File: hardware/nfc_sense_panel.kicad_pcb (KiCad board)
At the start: 4 copper layers, 105 x 103.3 mm, 538 parts, among them U1 TMP117AIDRVR, U2 RF430CL330HIRGTR‎, U3 ATtiny1626-MFR

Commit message: penel mousebite spacing
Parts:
- added KiKit_MB_10_9: NPTH, NPTH, F.Cu at (150.0, 27.0)
- added KiKit_MB_11_9: NPTH, NPTH, F.Cu at (147.0, 69.8)
- added KiKit_MB_12_9: NPTH, NPTH, F.Cu at (160.8, 47.1)
- added KiKit_MB_13_9: NPTH, NPTH, F.Cu at (179.4, 50.1)
- added KiKit_MB_14_9: NPTH, NPTH, F.Cu at (171.6, 27.0)
- added KiKit_MB_15_9: NPTH, NPTH, F.Cu at (168.6, 69.8)
- added KiKit_MB_16_9: NPTH, NPTH, F.Cu at (182.4, 47.1)
- added KiKit_MB_17_9: NPTH, NPTH, F.Cu at (193.2, 27.0)
- added KiKit_MB_18_9: NPTH, NPTH, F.Cu at (190.2, 69.8)
- added KiKit_MB_19_9: NPTH, NPTH, F.Cu at (114.6, 96.2)
- added KiKit_MB_1_9: NPTH, NPTH, F.Cu at (114.6, 50.1)
- added KiKit_MB_20_9: NPTH, NPTH, F.Cu at (106.8, 73.1)
- added KiKit_MB_21_9: NPTH, NPTH, F.Cu at (103.8, 116.0)
- added KiKit_MB_22_9: NPTH, NPTH, F.Cu at (117.6, 93.2)
- added KiKit_MB_23_9: NPTH, NPTH, F.Cu at (136.2, 96.2)
- added KiKit_MB_24_9: NPTH, NPTH, F.Cu at (128.4, 73.1)
- added KiKit_MB_25_9: NPTH, NPTH, F.Cu at (125.4, 116.0)
- added KiKit_MB_26_9: NPTH, NPTH, F.Cu at (139.2, 93.2)
- added KiKit_MB_27_9: NPTH, NPTH, F.Cu at (157.8, 96.2)
- added KiKit_MB_28_9: NPTH, NPTH, F.Cu at (150.0, 73.1)
- added KiKit_MB_29_9: NPTH, NPTH, F.Cu at (147.0, 116.0)
- added KiKit_MB_2_9: NPTH, NPTH, F.Cu at (106.8, 27.0)
- added KiKit_MB_30_9: NPTH, NPTH, F.Cu at (160.8, 93.2)
- added KiKit_MB_31_9: NPTH, NPTH, F.Cu at (179.4, 96.2)
- added KiKit_MB_32_9: NPTH, NPTH, F.Cu at (171.6, 73.1)
- added KiKit_MB_33_9: NPTH, NPTH, F.Cu at (168.6, 116.0)
- added KiKit_MB_34_9: NPTH, NPTH, F.Cu at (182.4, 93.2)
- added KiKit_MB_35_9: NPTH, NPTH, F.Cu at (193.2, 73.1)
- added KiKit_MB_36_9: NPTH, NPTH, F.Cu at (190.2, 116.0)
- added KiKit_MB_3_9: NPTH, NPTH, F.Cu at (103.8, 69.8)
- added KiKit_MB_4_9: NPTH, NPTH, F.Cu at (117.6, 47.1)
- added KiKit_MB_5_9: NPTH, NPTH, F.Cu at (136.2, 50.1)
- added KiKit_MB_6_9: NPTH, NPTH, F.Cu at (128.4, 27.0)
- added KiKit_MB_7_9: NPTH, NPTH, F.Cu at (125.4, 69.8)
- added KiKit_MB_8_9: NPTH, NPTH, F.Cu at (139.2, 47.1)
- added KiKit_MB_9_9: NPTH, NPTH, F.Cu at (157.8, 50.1)
- moved KiKit_MB_11_8 0.39 mm to (147.4, 70.0)
- moved KiKit_MB_18_8 0.39 mm to (190.6, 70.0)
- moved KiKit_MB_29_8 0.39 mm to (147.4, 116.1)
- moved KiKit_MB_36_8 0.39 mm to (190.6, 116.1)
- moved KiKit_MB_21_8 0.39 mm to (104.2, 116.1)
- moved KiKit_MB_25_8 0.39 mm to (125.8, 116.1)
- moved KiKit_MB_3_8 0.39 mm to (104.2, 70.0)
- moved KiKit_MB_7_8 0.39 mm to (125.8, 70.0)
- moved KiKit_MB_15_8 0.39 mm to (169.0, 70.0)
- moved KiKit_MB_33_8 0.39 mm to (169.0, 116.1)
- moved KiKit_MB_10_8 0.38 mm to (149.6, 27.0)
- moved KiKit_MB_12_8 0.38 mm to (160.8, 47.4)
- moved KiKit_MB_13_8 0.38 mm to (179.4, 49.7)
- moved KiKit_MB_14_8 0.38 mm to (171.2, 27.0)
- moved KiKit_MB_16_8 0.38 mm to (182.4, 47.4)
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
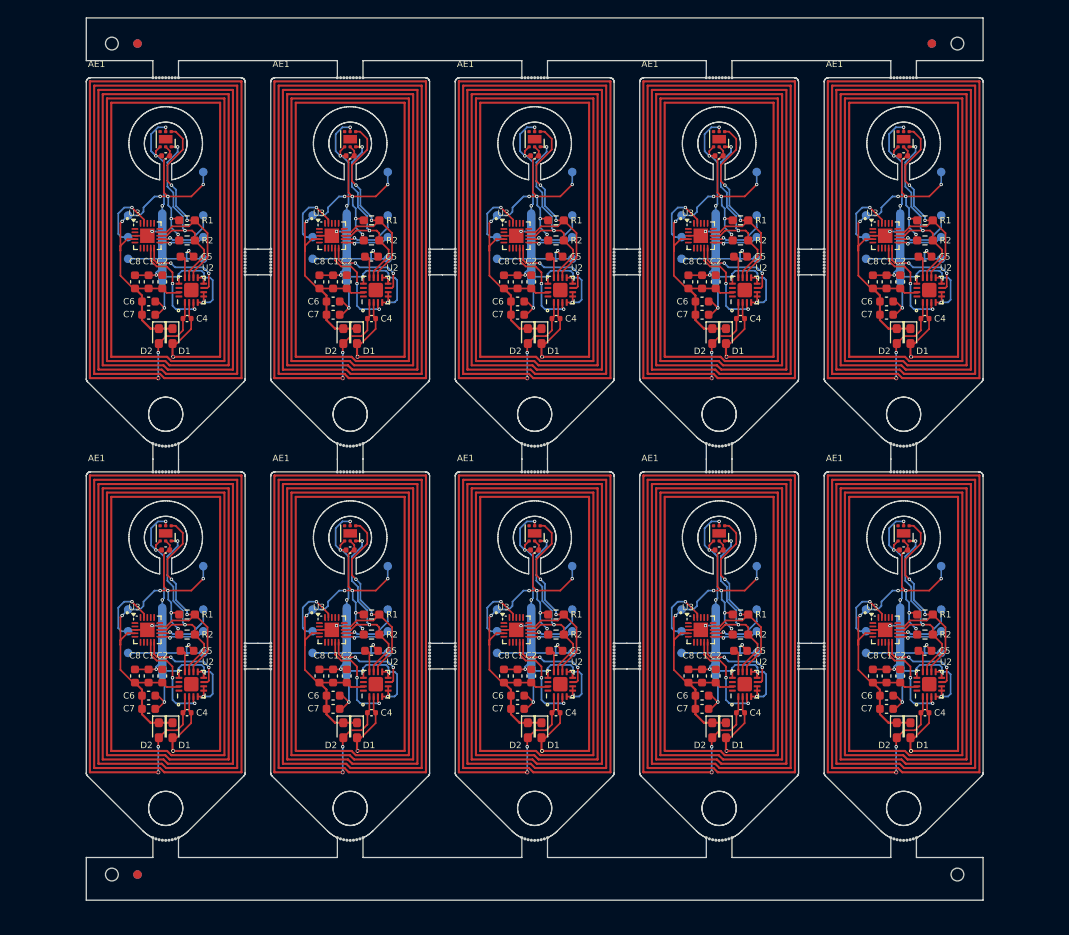
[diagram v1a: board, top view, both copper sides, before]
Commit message: new panel frame
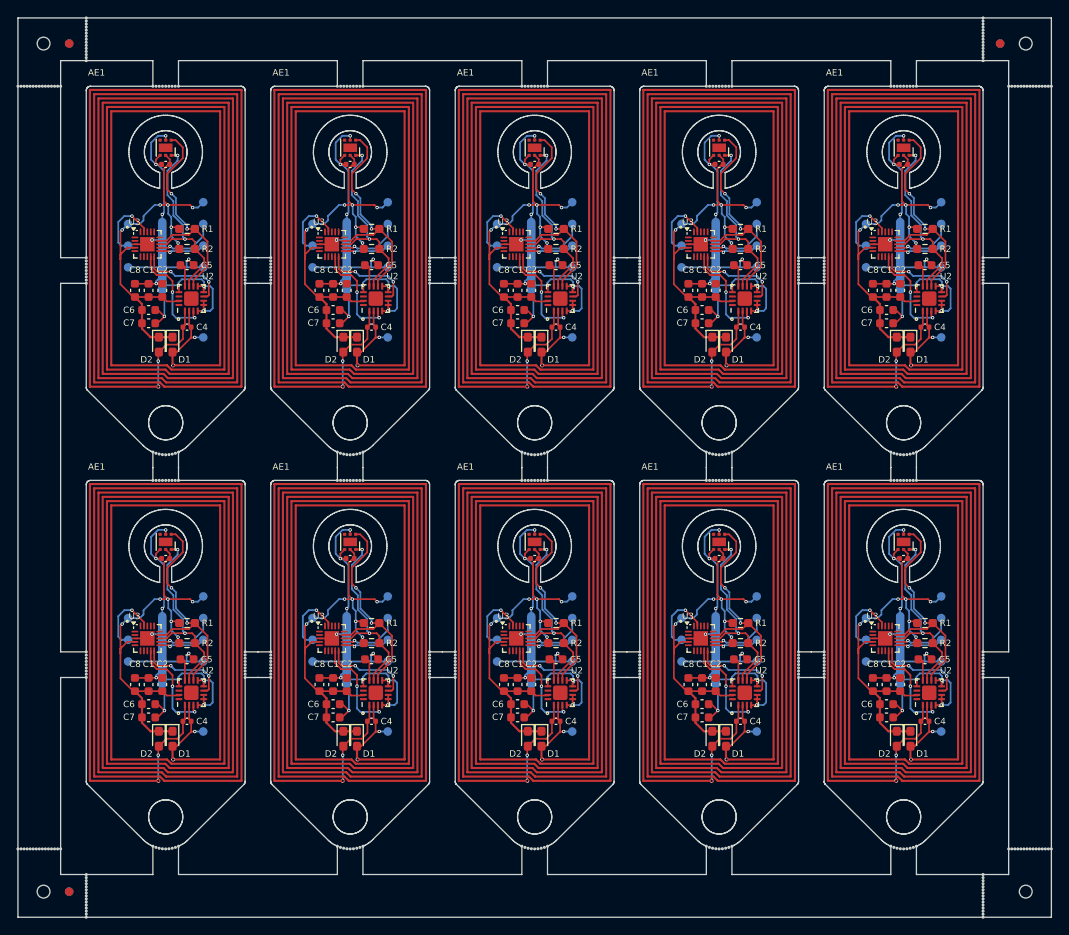
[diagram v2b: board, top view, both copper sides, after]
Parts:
- removed the AE1 at (182.7, 27.3)
- removed the AE1 at (96.3, 27.3)
- removed the AE1 at (182.7, 73.4)
- removed the AE1 at (117.9, 27.3)
- removed the AE1 at (139.5, 27.3)
- removed the AE1 at (139.5, 73.4)
- removed the AE1 at (117.9, 73.4)
- removed the AE1 at (161.1, 73.4)
- removed the AE1 at (161.1, 27.3)
- removed the AE1 at (96.3, 73.4)
- removed the C1 at (189.7, 50.9)
- removed the C1 at (146.5, 50.9)
- removed the C1 at (189.7, 97.0)
- removed the C1 at (124.9, 97.0)
- removed the C1 at (103.3, 50.9)
- removed the C1 at (168.1, 97.0)
- removed the C1 at (146.5, 97.0)
- removed the C1 at (103.3, 97.0)
- removed the C1 at (168.1, 50.9)
- removed the C1 at (124.9, 50.9)
- removed the C2 at (104.9, 97.0)
- removed the C2 at (169.7, 50.9)
- removed the C2 at (169.7, 97.0)
- removed the C2 at (191.3, 97.0)
- removed the C2 at (148.1, 97.0)
- removed the C2 at (191.3, 50.9)
- removed the C2 at (126.5, 50.9)
- removed the C2 at (126.5, 97.0)
- removed the C2 at (104.9, 50.9)
- removed the C2 at (148.1, 50.9)
- removed the C3 at (148.5, 36.2)
- removed the C3 at (170.1, 36.2)
- removed the C3 at (126.9, 36.2)
- removed the C3 at (148.5, 82.3)
- removed the C3 at (191.7, 36.2)
- removed the C3 at (105.3, 82.3)
- removed the C3 at (191.7, 82.3)
- removed the C3 at (105.3, 36.2)
- removed the C3 at (126.9, 82.3)
- removed the C3 at (170.1, 82.3)
- removed the C4 at (107.8, 55.2)
- removed the C4 at (129.4, 55.2)
- removed the C4 at (129.4, 101.3)
- removed the C4 at (172.6, 101.3)
- removed the C4 at (194.2, 55.2)
- removed the C4 at (172.6, 55.2)
- removed the C4 at (151.0, 55.2)
- removed the C4 at (151.0, 101.3)
- removed the C4 at (107.8, 101.3)
- removed the C4 at (194.2, 101.3)
- removed the C5 at (151.0, 48.0)
- removed the C5 at (129.4, 94.1)
- removed the C5 at (107.8, 94.1)
- removed the C5 at (172.6, 48.0)
- removed the C5 at (129.4, 48.0)
- removed the C5 at (172.6, 94.1)
- removed the C5 at (194.2, 94.1)
- removed the C5 at (194.2, 48.0)
- removed the C5 at (151.0, 94.1)
- removed the C5 at (107.8, 48.0)
- removed the C6 at (124.9, 53.2)
- removed the C6 at (103.3, 99.3)
- removed the C6 at (146.5, 53.2)
- removed the C6 at (168.1, 99.3)
- removed the C6 at (103.3, 53.2)
- removed the C6 at (168.1, 53.2)
- removed the C6 at (124.9, 99.3)
- removed the C6 at (146.5, 99.3)
- removed the C6 at (189.7, 99.3)
- removed the C6 at (189.7, 53.2)
- removed the C7 at (103.3, 54.8)
- removed the C7 at (146.5, 54.8)
- removed the C7 at (124.9, 54.8)
- removed the C7 at (168.1, 100.9)
- removed the C7 at (168.1, 54.8)
- removed the C7 at (103.3, 100.9)
- removed the C7 at (189.7, 100.9)
- removed the C7 at (124.9, 100.9)
- removed the C7 at (146.5, 100.9)
- removed the C7 at (189.7, 54.8)
- removed the C8 at (123.3, 50.9)
- removed the C8 at (144.9, 50.9)
- removed the C8 at (123.3, 97.0)
- removed the C8 at (101.7, 97.0)
- removed the C8 at (166.5, 50.9)
- removed the C8 at (188.1, 50.9)
- removed the C8 at (166.5, 97.0)
- removed the C8 at (188.1, 97.0)
- removed the C8 at (144.9, 97.0)
- removed the C8 at (101.7, 50.9)
- removed the D1 at (192.5, 103.4)
- removed the D1 at (127.7, 103.4)
- removed the D1 at (106.1, 57.3)
- removed the D1 at (170.9, 103.4)
- removed the D1 at (127.7, 57.3)
- removed the D1 at (192.5, 57.3)
- removed the D1 at (106.1, 103.4)
- removed the D1 at (149.3, 57.3)
- removed the D1 at (149.3, 103.4)
- removed the D1 at (170.9, 57.3)
- removed the D2 at (190.9, 103.4)
- removed the D2 at (147.7, 57.3)
- removed the D2 at (169.3, 57.3)
- removed the D2 at (126.1, 103.4)
- removed the D2 at (104.5, 103.4)
- removed the D2 at (169.3, 103.4)
- removed the D2 at (190.9, 57.3)
- removed the D2 at (104.5, 57.3)
- removed the D2 at (147.7, 103.4)
- removed the D2 at (126.1, 57.3)
- removed the GND1 at (187.3, 94.3)
- removed the GND1 at (122.5, 94.3)
- removed the GND1 at (100.9, 94.3)
- removed the GND1 at (187.3, 48.2)
- removed the GND1 at (144.1, 48.2)
- removed the GND1 at (144.1, 94.3)
- removed the GND1 at (165.7, 48.2)
- removed the GND1 at (100.9, 48.2)
- removed the GND1 at (165.7, 94.3)
- removed the GND1 at (122.5, 48.2)
- removed the QR_ref1 at (191.7, 54.2)
- removed the QR_ref1 at (126.9, 100.3)
- removed the QR_ref1 at (170.1, 100.3)
- removed the QR_ref1 at (105.3, 54.2)
- removed the QR_ref1 at (191.7, 100.3)
- removed the QR_ref1 at (170.1, 54.2)
- removed the QR_ref1 at (148.5, 100.3)
- removed the QR_ref1 at (148.5, 54.2)
- removed the QR_ref1 at (105.3, 100.3)
- removed the QR_ref1 at (126.9, 54.2)
- removed the R1 at (107.8, 89.8)
- removed the R1 at (107.8, 43.7)
- removed the R1 at (172.6, 43.7)
- removed the R1 at (194.2, 43.7)
- removed the R1 at (151.0, 43.7)
- removed the R1 at (129.4, 89.8)
- removed the R1 at (172.6, 89.8)
- removed the R1 at (194.2, 89.8)
- removed the R1 at (129.4, 43.7)
- removed the R1 at (151.0, 89.8)
- removed the R2 at (194.2, 46.1)
- removed the R2 at (107.8, 92.2)
- removed the R2 at (194.2, 92.2)
- removed the R2 at (151.0, 92.2)
- removed the R2 at (129.4, 46.1)
- removed the R2 at (129.4, 92.2)
- removed the R2 at (107.8, 46.1)
- removed the R2 at (172.6, 46.1)
- removed the R2 at (151.0, 46.1)
- removed the R2 at (172.6, 92.2)
- removed the TP1 at (131.3, 45.7)
- removed the TP1 at (109.7, 45.7)
- removed the TP1 at (109.7, 91.8)
- removed the TP1 at (174.5, 91.8)
- removed the TP1 at (152.9, 91.8)
- removed the TP1 at (196.1, 45.7)
- removed the TP1 at (131.3, 91.8)
- removed the TP1 at (152.9, 45.7)
- removed the TP1 at (196.1, 91.8)
- removed the TP1 at (174.5, 45.7)
- removed the TP2 at (174.5, 43.1)
- removed the TP2 at (131.3, 43.1)
- removed the TP2 at (152.9, 43.1)
- removed the TP2 at (152.9, 89.3)
- removed the TP2 at (131.3, 89.3)
- removed the TP2 at (109.7, 89.3)
- removed the TP2 at (196.1, 43.1)
- removed the TP2 at (109.7, 43.1)
- removed the TP2 at (174.5, 89.3)
- removed the TP2 at (196.1, 89.3)
- removed the TP3 at (109.7, 48.2)
- removed the TP3 at (196.1, 94.3)
- removed the TP3 at (131.3, 48.2)
- removed the TP3 at (152.9, 48.2)
- removed the TP3 at (131.3, 94.3)
- removed the TP3 at (109.7, 94.3)
- removed the TP3 at (152.9, 94.3)
- removed the TP3 at (196.1, 48.2)
- removed the TP3 at (174.5, 48.2)
- removed the TP3 at (174.5, 94.3)
- removed the TP4 at (174.5, 38.0)
- removed the TP4 at (196.1, 38.0)
- removed the TP4 at (174.5, 84.2)
- removed the TP4 at (152.9, 38.0)
- removed the TP4 at (109.7, 38.0)
- removed the TP4 at (131.3, 38.0)
- removed the TP4 at (109.7, 84.2)
- removed the TP4 at (152.9, 84.2)
- removed the TP4 at (131.3, 84.2)
- removed the TP4 at (196.1, 84.2)
- removed the U1 at (105.3, 80.3)
- removed the U1 at (191.7, 34.2)
- removed the U1 at (126.9, 80.3)
- removed the U1 at (170.1, 34.2)
- removed the U1 at (105.3, 34.2)
- removed the U1 at (148.5, 34.2)
- removed the U1 at (170.1, 80.3)
- removed the U1 at (191.7, 80.3)
- removed the U1 at (126.9, 34.2)
- removed the U1 at (148.5, 80.3)
- removed the U2 at (129.9, 51.9)
- removed the U2 at (194.7, 98.0)
- removed the U2 at (129.9, 98.0)
- removed the U2 at (108.3, 98.0)
- removed the U2 at (173.1, 51.9)
- removed the U2 at (108.3, 51.9)
- removed the U2 at (173.1, 98.0)
- removed the U2 at (151.5, 98.0)
- removed the U2 at (194.7, 51.9)
- removed the U2 at (151.5, 51.9)
- removed the U3 at (146.4, 91.6)
- removed the U3 at (189.6, 45.5)
- removed the U3 at (124.7, 45.5)
- removed the U3 at (168.0, 45.5)
- removed the U3 at (146.4, 45.5)
- removed the U3 at (103.1, 45.5)
- removed the U3 at (189.6, 91.6)
- removed the U3 at (103.1, 91.6)
- removed the U3 at (168.0, 91.6)
- removed the U3 at (124.7, 91.6)
- removed the UPDI1 at (144.1, 45.7)
- removed the UPDI1 at (100.9, 91.8)
- removed the UPDI1 at (165.7, 91.8)
- removed the UPDI1 at (187.3, 45.7)
- removed the UPDI1 at (122.5, 91.8)
- removed the UPDI1 at (122.5, 45.7)
- removed the UPDI1 at (187.3, 91.8)
- removed the UPDI1 at (100.9, 45.7)
- removed the UPDI1 at (144.1, 91.8)
- removed the UPDI1 at (165.7, 45.7)
- removed the VCC1 at (100.9, 89.3)
- removed the VCC1 at (165.7, 89.3)
- removed the VCC1 at (122.5, 43.1)
- removed the VCC1 at (187.3, 43.1)
- removed the VCC1 at (122.5, 89.3)
- removed the VCC1 at (187.3, 89.3)
- removed the VCC1 at (144.1, 89.3)
- removed the VCC1 at (100.9, 43.1)
- removed the VCC1 at (144.1, 43.1)
- removed the VCC1 at (165.7, 43.1)
- added AE1: Antenna_Dipole, unsurv_offline_pcb_footprints:35_18_1_9nH, F.Cu at (161.1, 74.4)
- added AE1: Antenna_Dipole, unsurv_offline_pcb_footprints:35_18_1_9nH, F.Cu at (96.3, 28.3)
- added AE1: Antenna_Dipole, unsurv_offline_pcb_footprints:35_18_1_9nH, F.Cu at (117.9, 74.4)
- added AE1: Antenna_Dipole, unsurv_offline_pcb_footprints:35_18_1_9nH, F.Cu at (139.5, 28.3)
- added AE1: Antenna_Dipole, unsurv_offline_pcb_footprints:35_18_1_9nH, F.Cu at (139.5, 74.4)
- added AE1: Antenna_Dipole, unsurv_offline_pcb_footprints:35_18_1_9nH, F.Cu at (117.9, 28.3)
- added AE1: Antenna_Dipole, unsurv_offline_pcb_footprints:35_18_1_9nH, F.Cu at (161.1, 28.3)
- added AE1: Antenna_Dipole, unsurv_offline_pcb_footprints:35_18_1_9nH, F.Cu at (182.7, 74.4)
- added AE1: Antenna_Dipole, unsurv_offline_pcb_footprints:35_18_1_9nH, F.Cu at (96.3, 74.4)
- added AE1: Antenna_Dipole, unsurv_offline_pcb_footprints:35_18_1_9nH, F.Cu at (182.7, 28.3)
- added C1: 1 uF, Capacitor_SMD:C_0603_1608Metric, F.Cu at (168.1, 98.0)
- added C1: 1 uF, Capacitor_SMD:C_0603_1608Metric, F.Cu at (189.7, 51.9)
- added C1: 1 uF, Capacitor_SMD:C_0603_1608Metric, F.Cu at (103.3, 98.0)
- added C1: 1 uF, Capacitor_SMD:C_0603_1608Metric, F.Cu at (146.5, 98.0)
- added C1: 1 uF, Capacitor_SMD:C_0603_1608Metric, F.Cu at (189.7, 98.0)
- added C1: 1 uF, Capacitor_SMD:C_0603_1608Metric, F.Cu at (124.9, 51.9)
- added C1: 1 uF, Capacitor_SMD:C_0603_1608Metric, F.Cu at (124.9, 98.0)
- added C1: 1 uF, Capacitor_SMD:C_0603_1608Metric, F.Cu at (146.5, 51.9)
- added C1: 1 uF, Capacitor_SMD:C_0603_1608Metric, F.Cu at (168.1, 51.9)
- added C1: 1 uF, Capacitor_SMD:C_0603_1608Metric, F.Cu at (103.3, 51.9)
- added C2: 0.1 uF, Capacitor_SMD:C_0603_1608Metric, F.Cu at (169.7, 98.0)
- added C2: 0.1 uF, Capacitor_SMD:C_0603_1608Metric, F.Cu at (191.3, 98.0)
- added C2: 0.1 uF, Capacitor_SMD:C_0603_1608Metric, F.Cu at (191.3, 51.9)
- added C2: 0.1 uF, Capacitor_SMD:C_0603_1608Metric, F.Cu at (126.5, 98.0)
- added C2: 0.1 uF, Capacitor_SMD:C_0603_1608Metric, F.Cu at (148.1, 98.0)
- added C2: 0.1 uF, Capacitor_SMD:C_0603_1608Metric, F.Cu at (169.7, 51.9)
- added C2: 0.1 uF, Capacitor_SMD:C_0603_1608Metric, F.Cu at (104.9, 98.0)
- added C2: 0.1 uF, Capacitor_SMD:C_0603_1608Metric, F.Cu at (126.5, 51.9)
- added C2: 0.1 uF, Capacitor_SMD:C_0603_1608Metric, F.Cu at (104.9, 51.9)
- added C2: 0.1 uF, Capacitor_SMD:C_0603_1608Metric, F.Cu at (148.1, 51.9)
- added C3: 0.1 uF, Capacitor_SMD:C_0402_1005Metric, F.Cu at (126.9, 37.2)
- added C3: 0.1 uF, Capacitor_SMD:C_0402_1005Metric, F.Cu at (170.1, 37.2)
- added C3: 0.1 uF, Capacitor_SMD:C_0402_1005Metric, F.Cu at (148.5, 37.2)
- added C3: 0.1 uF, Capacitor_SMD:C_0402_1005Metric, F.Cu at (105.3, 83.3)
- added C3: 0.1 uF, Capacitor_SMD:C_0402_1005Metric, F.Cu at (191.7, 37.2)
- added C3: 0.1 uF, Capacitor_SMD:C_0402_1005Metric, F.Cu at (126.9, 83.3)
- added C3: 0.1 uF, Capacitor_SMD:C_0402_1005Metric, F.Cu at (191.7, 83.3)
- added C3: 0.1 uF, Capacitor_SMD:C_0402_1005Metric, F.Cu at (170.1, 83.3)
- added C3: 0.1 uF, Capacitor_SMD:C_0402_1005Metric, F.Cu at (148.5, 83.3)
- added C3: 0.1 uF, Capacitor_SMD:C_0402_1005Metric, F.Cu at (105.3, 37.2)
- added C4: 36pF, Capacitor_SMD:C_0402_1005Metric, F.Cu at (194.2, 56.2)
- added C4: 36pF, Capacitor_SMD:C_0402_1005Metric, F.Cu at (172.6, 56.2)
- added C4: 36pF, Capacitor_SMD:C_0402_1005Metric, F.Cu at (151.0, 56.2)
- added C4: 36pF, Capacitor_SMD:C_0402_1005Metric, F.Cu at (172.6, 102.3)
- added C4: 36pF, Capacitor_SMD:C_0402_1005Metric, F.Cu at (107.8, 56.2)
- added C4: 36pF, Capacitor_SMD:C_0402_1005Metric, F.Cu at (151.0, 102.3)
- added C4: 36pF, Capacitor_SMD:C_0402_1005Metric, F.Cu at (194.2, 102.3)
- added C4: 36pF, Capacitor_SMD:C_0402_1005Metric, F.Cu at (129.4, 102.3)
- added C4: 36pF, Capacitor_SMD:C_0402_1005Metric, F.Cu at (107.8, 102.3)
- added C4: 36pF, Capacitor_SMD:C_0402_1005Metric, F.Cu at (129.4, 56.2)
- added C5: 0.47 uF, Capacitor_SMD:C_0603_1608Metric, F.Cu at (129.4, 95.1)
- added C5: 0.47 uF, Capacitor_SMD:C_0603_1608Metric, F.Cu at (151.0, 95.1)
- added C5: 0.47 uF, Capacitor_SMD:C_0603_1608Metric, F.Cu at (107.8, 95.1)
- added C5: 0.47 uF, Capacitor_SMD:C_0603_1608Metric, F.Cu at (107.8, 49.0)
- added C5: 0.47 uF, Capacitor_SMD:C_0603_1608Metric, F.Cu at (172.6, 49.0)
- added C5: 0.47 uF, Capacitor_SMD:C_0603_1608Metric, F.Cu at (194.2, 49.0)
- added C5: 0.47 uF, Capacitor_SMD:C_0603_1608Metric, F.Cu at (172.6, 95.1)
- added C5: 0.47 uF, Capacitor_SMD:C_0603_1608Metric, F.Cu at (151.0, 49.0)
- added C5: 0.47 uF, Capacitor_SMD:C_0603_1608Metric, F.Cu at (194.2, 95.1)
- added C5: 0.47 uF, Capacitor_SMD:C_0603_1608Metric, F.Cu at (129.4, 49.0)
- added C6: 47uF, Capacitor_SMD:C_0603_1608Metric, F.Cu at (103.3, 54.2)
- added C6: 47uF, Capacitor_SMD:C_0603_1608Metric, F.Cu at (189.7, 54.2)
- added C6: 47uF, Capacitor_SMD:C_0603_1608Metric, F.Cu at (146.5, 54.2)
- added C6: 47uF, Capacitor_SMD:C_0603_1608Metric, F.Cu at (168.1, 100.3)
- added C6: 47uF, Capacitor_SMD:C_0603_1608Metric, F.Cu at (103.3, 100.3)
- added C6: 47uF, Capacitor_SMD:C_0603_1608Metric, F.Cu at (124.9, 100.3)
- added C6: 47uF, Capacitor_SMD:C_0603_1608Metric, F.Cu at (146.5, 100.3)
- added C6: 47uF, Capacitor_SMD:C_0603_1608Metric, F.Cu at (124.9, 54.2)
- added C6: 47uF, Capacitor_SMD:C_0603_1608Metric, F.Cu at (189.7, 100.3)
- added C6: 47uF, Capacitor_SMD:C_0603_1608Metric, F.Cu at (168.1, 54.2)
- added C7: 47uF, Capacitor_SMD:C_0603_1608Metric, F.Cu at (103.3, 55.8)
- added C7: 47uF, Capacitor_SMD:C_0603_1608Metric, F.Cu at (168.1, 55.8)
- added C7: 47uF, Capacitor_SMD:C_0603_1608Metric, F.Cu at (124.9, 101.9)
- added C7: 47uF, Capacitor_SMD:C_0603_1608Metric, F.Cu at (189.7, 101.9)
- added C7: 47uF, Capacitor_SMD:C_0603_1608Metric, F.Cu at (189.7, 55.8)
- added C7: 47uF, Capacitor_SMD:C_0603_1608Metric, F.Cu at (124.9, 55.8)
- added C7: 47uF, Capacitor_SMD:C_0603_1608Metric, F.Cu at (146.5, 55.8)
- added C7: 47uF, Capacitor_SMD:C_0603_1608Metric, F.Cu at (168.1, 101.9)
- added C7: 47uF, Capacitor_SMD:C_0603_1608Metric, F.Cu at (146.5, 101.9)
- added C7: 47uF, Capacitor_SMD:C_0603_1608Metric, F.Cu at (103.3, 101.9)
- added C8: 0.1 uF, Capacitor_SMD:C_0603_1608Metric, F.Cu at (144.9, 51.9)
- added C8: 0.1 uF, Capacitor_SMD:C_0603_1608Metric, F.Cu at (101.7, 51.9)
- added C8: 0.1 uF, Capacitor_SMD:C_0603_1608Metric, F.Cu at (144.9, 98.0)
- added C8: 0.1 uF, Capacitor_SMD:C_0603_1608Metric, F.Cu at (188.1, 51.9)
- added C8: 0.1 uF, Capacitor_SMD:C_0603_1608Metric, F.Cu at (101.7, 98.0)
- added C8: 0.1 uF, Capacitor_SMD:C_0603_1608Metric, F.Cu at (166.5, 51.9)
- added C8: 0.1 uF, Capacitor_SMD:C_0603_1608Metric, F.Cu at (123.3, 98.0)
- added C8: 0.1 uF, Capacitor_SMD:C_0603_1608Metric, F.Cu at (188.1, 98.0)
- added C8: 0.1 uF, Capacitor_SMD:C_0603_1608Metric, F.Cu at (123.3, 51.9)
- added C8: 0.1 uF, Capacitor_SMD:C_0603_1608Metric, F.Cu at (166.5, 98.0)
- added D1: CDBU0130L, Diode_SMD:D_0603_1608Metric_Pad1.05x0.95mm_HandSolder, F.Cu at (106.1, 104.4)
- added D1: CDBU0130L, Diode_SMD:D_0603_1608Metric_Pad1.05x0.95mm_HandSolder, F.Cu at (127.7, 104.4)
- added D1: CDBU0130L, Diode_SMD:D_0603_1608Metric_Pad1.05x0.95mm_HandSolder, F.Cu at (149.3, 104.4)
- added D1: CDBU0130L, Diode_SMD:D_0603_1608Metric_Pad1.05x0.95mm_HandSolder, F.Cu at (106.1, 58.3)
- added D1: CDBU0130L, Diode_SMD:D_0603_1608Metric_Pad1.05x0.95mm_HandSolder, F.Cu at (170.9, 58.3)
- added D1: CDBU0130L, Diode_SMD:D_0603_1608Metric_Pad1.05x0.95mm_HandSolder, F.Cu at (192.5, 104.4)
- added D1: CDBU0130L, Diode_SMD:D_0603_1608Metric_Pad1.05x0.95mm_HandSolder, F.Cu at (149.3, 58.3)
- added D1: CDBU0130L, Diode_SMD:D_0603_1608Metric_Pad1.05x0.95mm_HandSolder, F.Cu at (127.7, 58.3)
- added D1: CDBU0130L, Diode_SMD:D_0603_1608Metric_Pad1.05x0.95mm_HandSolder, F.Cu at (192.5, 58.3)
- added D1: CDBU0130L, Diode_SMD:D_0603_1608Metric_Pad1.05x0.95mm_HandSolder, F.Cu at (170.9, 104.4)
- added D2: CDBU0130L, Diode_SMD:D_0603_1608Metric_Pad1.05x0.95mm_HandSolder, F.Cu at (147.7, 58.3)
- added D2: CDBU0130L, Diode_SMD:D_0603_1608Metric_Pad1.05x0.95mm_HandSolder, F.Cu at (169.3, 58.3)
- added D2: CDBU0130L, Diode_SMD:D_0603_1608Metric_Pad1.05x0.95mm_HandSolder, F.Cu at (147.7, 104.4)
- added D2: CDBU0130L, Diode_SMD:D_0603_1608Metric_Pad1.05x0.95mm_HandSolder, F.Cu at (126.1, 104.4)
- added D2: CDBU0130L, Diode_SMD:D_0603_1608Metric_Pad1.05x0.95mm_HandSolder, F.Cu at (190.9, 104.4)
- added D2: CDBU0130L, Diode_SMD:D_0603_1608Metric_Pad1.05x0.95mm_HandSolder, F.Cu at (104.5, 104.4)
- added D2: CDBU0130L, Diode_SMD:D_0603_1608Metric_Pad1.05x0.95mm_HandSolder, F.Cu at (104.5, 58.3)
- added D2: CDBU0130L, Diode_SMD:D_0603_1608Metric_Pad1.05x0.95mm_HandSolder, F.Cu at (126.1, 58.3)
- added D2: CDBU0130L, Diode_SMD:D_0603_1608Metric_Pad1.05x0.95mm_HandSolder, F.Cu at (190.9, 58.3)
- added D2: CDBU0130L, Diode_SMD:D_0603_1608Metric_Pad1.05x0.95mm_HandSolder, F.Cu at (169.3, 104.4)
- added GND1: TestPoint, TestPoint:TestPoint_Pad_D1.0mm, B.Cu at (100.9, 49.2)
- added GND1: TestPoint, TestPoint:TestPoint_Pad_D1.0mm, B.Cu at (122.5, 95.3)
- added GND1: TestPoint, TestPoint:TestPoint_Pad_D1.0mm, B.Cu at (165.7, 95.3)
- added GND1: TestPoint, TestPoint:TestPoint_Pad_D1.0mm, B.Cu at (122.5, 49.2)
- added GND1: TestPoint, TestPoint:TestPoint_Pad_D1.0mm, B.Cu at (100.9, 95.3)
- added GND1: TestPoint, TestPoint:TestPoint_Pad_D1.0mm, B.Cu at (187.3, 49.2)
- added GND1: TestPoint, TestPoint:TestPoint_Pad_D1.0mm, B.Cu at (165.7, 49.2)
- added GND1: TestPoint, TestPoint:TestPoint_Pad_D1.0mm, B.Cu at (144.1, 49.2)
- added GND1: TestPoint, TestPoint:TestPoint_Pad_D1.0mm, B.Cu at (187.3, 95.3)
- added GND1: TestPoint, TestPoint:TestPoint_Pad_D1.0mm, B.Cu at (144.1, 95.3)
- added KiKit_MB_37_1: NPTH, NPTH, F.Cu at (182.4, 97.2)
- added KiKit_MB_37_2: NPTH, NPTH, F.Cu at (182.4, 96.8)
- added KiKit_MB_37_3: NPTH, NPTH, F.Cu at (182.4, 96.5)
- added KiKit_MB_37_4: NPTH, NPTH, F.Cu at (182.4, 96.1)
- added KiKit_MB_37_5: NPTH, NPTH, F.Cu at (182.4, 95.7)
- added KiKit_MB_37_6: NPTH, NPTH, F.Cu at (182.4, 95.3)
- added KiKit_MB_37_7: NPTH, NPTH, F.Cu at (182.4, 95.0)
- added KiKit_MB_37_8: NPTH, NPTH, F.Cu at (182.4, 94.6)
- added KiKit_MB_37_9: NPTH, NPTH, F.Cu at (182.4, 94.2)
- added KiKit_MB_38_1: NPTH, NPTH, F.Cu at (201.0, 94.2)
- added KiKit_MB_38_2: NPTH, NPTH, F.Cu at (201.0, 94.6)
- added KiKit_MB_38_3: NPTH, NPTH, F.Cu at (201.0, 95.0)
- added KiKit_MB_38_4: NPTH, NPTH, F.Cu at (201.0, 95.3)
- added KiKit_MB_38_5: NPTH, NPTH, F.Cu at (201.0, 95.7)
- added KiKit_MB_38_6: NPTH, NPTH, F.Cu at (201.0, 96.1)
- added KiKit_MB_38_7: NPTH, NPTH, F.Cu at (201.0, 96.5)
- added KiKit_MB_38_8: NPTH, NPTH, F.Cu at (201.0, 96.8)
- added KiKit_MB_38_9: NPTH, NPTH, F.Cu at (201.0, 97.2)
- added KiKit_MB_39_1: NPTH, NPTH, F.Cu at (190.2, 74.1)
- added KiKit_MB_39_2: NPTH, NPTH, F.Cu at (190.6, 74.1)
- added KiKit_MB_39_3: NPTH, NPTH, F.Cu at (191.0, 74.1)
- added KiKit_MB_39_4: NPTH, NPTH, F.Cu at (191.3, 74.1)
- added KiKit_MB_39_5: NPTH, NPTH, F.Cu at (191.7, 74.1)
- added KiKit_MB_39_6: NPTH, NPTH, F.Cu at (192.1, 74.1)
- added KiKit_MB_39_7: NPTH, NPTH, F.Cu at (192.5, 74.1)
- added KiKit_MB_39_8: NPTH, NPTH, F.Cu at (192.8, 74.1)
- added KiKit_MB_39_9: NPTH, NPTH, F.Cu at (193.2, 74.1)
- added KiKit_MB_40_1: NPTH, NPTH, F.Cu at (193.2, 117.0)
- added KiKit_MB_40_2: NPTH, NPTH, F.Cu at (192.8, 117.1)
- added KiKit_MB_40_3: NPTH, NPTH, F.Cu at (192.5, 117.2)
- added KiKit_MB_40_4: NPTH, NPTH, F.Cu at (192.1, 117.3)
- added KiKit_MB_40_5: NPTH, NPTH, F.Cu at (191.7, 117.3)
- added KiKit_MB_40_6: NPTH, NPTH, F.Cu at (191.3, 117.3)
- added KiKit_MB_40_7: NPTH, NPTH, F.Cu at (190.9, 117.2)
- added KiKit_MB_40_8: NPTH, NPTH, F.Cu at (190.6, 117.1)
- added KiKit_MB_40_9: NPTH, NPTH, F.Cu at (190.2, 117.0)
- added KiKit_MB_41_1: NPTH, NPTH, F.Cu at (96.0, 20.0)
- added KiKit_MB_41_10: NPTH, NPTH, F.Cu at (96.0, 23.2)
- added KiKit_MB_41_11: NPTH, NPTH, F.Cu at (96.0, 23.6)
- added KiKit_MB_41_12: NPTH, NPTH, F.Cu at (96.0, 23.9)
- added KiKit_MB_41_13: NPTH, NPTH, F.Cu at (96.0, 24.3)
- added KiKit_MB_41_14: NPTH, NPTH, F.Cu at (96.0, 24.6)
- added KiKit_MB_41_15: NPTH, NPTH, F.Cu at (96.0, 25.0)
- added KiKit_MB_41_2: NPTH, NPTH, F.Cu at (96.0, 20.4)
- added KiKit_MB_41_3: NPTH, NPTH, F.Cu at (96.0, 20.7)
- added KiKit_MB_41_4: NPTH, NPTH, F.Cu at (96.0, 21.1)
- added KiKit_MB_41_5: NPTH, NPTH, F.Cu at (96.0, 21.4)
- added KiKit_MB_41_6: NPTH, NPTH, F.Cu at (96.0, 21.8)
- added KiKit_MB_41_7: NPTH, NPTH, F.Cu at (96.0, 22.1)
- added KiKit_MB_41_8: NPTH, NPTH, F.Cu at (96.0, 22.5)
- added KiKit_MB_41_9: NPTH, NPTH, F.Cu at (96.0, 22.9)
- added KiKit_MB_42_1: NPTH, NPTH, F.Cu at (201.0, 20.0)
- added KiKit_MB_42_10: NPTH, NPTH, F.Cu at (201.0, 23.2)
- added KiKit_MB_42_11: NPTH, NPTH, F.Cu at (201.0, 23.6)
- added KiKit_MB_42_12: NPTH, NPTH, F.Cu at (201.0, 23.9)
- added KiKit_MB_42_13: NPTH, NPTH, F.Cu at (201.0, 24.3)
- added KiKit_MB_42_14: NPTH, NPTH, F.Cu at (201.0, 24.6)
- added KiKit_MB_42_15: NPTH, NPTH, F.Cu at (201.0, 25.0)
- added KiKit_MB_42_2: NPTH, NPTH, F.Cu at (201.0, 20.4)
- added KiKit_MB_42_3: NPTH, NPTH, F.Cu at (201.0, 20.7)
- added KiKit_MB_42_4: NPTH, NPTH, F.Cu at (201.0, 21.1)
- added KiKit_MB_42_5: NPTH, NPTH, F.Cu at (201.0, 21.4)
- added KiKit_MB_42_6: NPTH, NPTH, F.Cu at (201.0, 21.8)
- added KiKit_MB_42_7: NPTH, NPTH, F.Cu at (201.0, 22.1)
- added KiKit_MB_42_8: NPTH, NPTH, F.Cu at (201.0, 22.5)
- added KiKit_MB_42_9: NPTH, NPTH, F.Cu at (201.0, 22.9)
- added KiKit_MB_43_1: NPTH, NPTH, F.Cu at (96.0, 120.3)
- added KiKit_MB_43_10: NPTH, NPTH, F.Cu at (96.0, 123.5)
- added KiKit_MB_43_11: NPTH, NPTH, F.Cu at (96.0, 123.9)
- added KiKit_MB_43_12: NPTH, NPTH, F.Cu at (96.0, 124.2)
- added KiKit_MB_43_13: NPTH, NPTH, F.Cu at (96.0, 124.6)
- added KiKit_MB_43_14: NPTH, NPTH, F.Cu at (96.0, 124.9)
- added KiKit_MB_43_15: NPTH, NPTH, F.Cu at (96.0, 125.3)
- added KiKit_MB_43_2: NPTH, NPTH, F.Cu at (96.0, 120.7)
- added KiKit_MB_43_3: NPTH, NPTH, F.Cu at (96.0, 121.0)
- added KiKit_MB_43_4: NPTH, NPTH, F.Cu at (96.0, 121.4)
- added KiKit_MB_43_5: NPTH, NPTH, F.Cu at (96.0, 121.7)
- added KiKit_MB_43_6: NPTH, NPTH, F.Cu at (96.0, 122.1)
- added KiKit_MB_43_7: NPTH, NPTH, F.Cu at (96.0, 122.4)
- added KiKit_MB_43_8: NPTH, NPTH, F.Cu at (96.0, 122.8)
- added KiKit_MB_43_9: NPTH, NPTH, F.Cu at (96.0, 123.2)
- added KiKit_MB_44_1: NPTH, NPTH, F.Cu at (201.0, 120.3)
- added KiKit_MB_44_10: NPTH, NPTH, F.Cu at (201.0, 123.5)
- added KiKit_MB_44_11: NPTH, NPTH, F.Cu at (201.0, 123.9)
- added KiKit_MB_44_12: NPTH, NPTH, F.Cu at (201.0, 124.2)
- added KiKit_MB_44_13: NPTH, NPTH, F.Cu at (201.0, 124.6)
- added KiKit_MB_44_14: NPTH, NPTH, F.Cu at (201.0, 124.9)
- added KiKit_MB_44_15: NPTH, NPTH, F.Cu at (201.0, 125.3)
- added KiKit_MB_44_2: NPTH, NPTH, F.Cu at (201.0, 120.7)
- added KiKit_MB_44_3: NPTH, NPTH, F.Cu at (201.0, 121.0)
- added KiKit_MB_44_4: NPTH, NPTH, F.Cu at (201.0, 121.4)
- added KiKit_MB_44_5: NPTH, NPTH, F.Cu at (201.0, 121.7)
- added KiKit_MB_44_6: NPTH, NPTH, F.Cu at (201.0, 122.1)
- added KiKit_MB_44_7: NPTH, NPTH, F.Cu at (201.0, 122.4)
- added KiKit_MB_44_8: NPTH, NPTH, F.Cu at (201.0, 122.8)
- added KiKit_MB_44_9: NPTH, NPTH, F.Cu at (201.0, 123.2)
- added KiKit_MB_45_1: NPTH, NPTH, F.Cu at (88.0, 28.0)
- added KiKit_MB_45_10: NPTH, NPTH, F.Cu at (91.2, 28.0)
- added KiKit_MB_45_11: NPTH, NPTH, F.Cu at (91.6, 28.0)
- added KiKit_MB_45_12: NPTH, NPTH, F.Cu at (91.9, 28.0)
- added KiKit_MB_45_13: NPTH, NPTH, F.Cu at (92.3, 28.0)
- added KiKit_MB_45_14: NPTH, NPTH, F.Cu at (92.6, 28.0)
- added KiKit_MB_45_15: NPTH, NPTH, F.Cu at (93.0, 28.0)
- added KiKit_MB_45_2: NPTH, NPTH, F.Cu at (88.4, 28.0)
- added KiKit_MB_45_3: NPTH, NPTH, F.Cu at (88.7, 28.0)
- added KiKit_MB_45_4: NPTH, NPTH, F.Cu at (89.1, 28.0)
- added KiKit_MB_45_5: NPTH, NPTH, F.Cu at (89.4, 28.0)
- added KiKit_MB_45_6: NPTH, NPTH, F.Cu at (89.8, 28.0)
- added KiKit_MB_45_7: NPTH, NPTH, F.Cu at (90.1, 28.0)
- added KiKit_MB_45_8: NPTH, NPTH, F.Cu at (90.5, 28.0)
- added KiKit_MB_45_9: NPTH, NPTH, F.Cu at (90.9, 28.0)
- added KiKit_MB_46_1: NPTH, NPTH, F.Cu at (88.0, 117.3)
- added KiKit_MB_46_10: NPTH, NPTH, F.Cu at (91.2, 117.3)
- added KiKit_MB_46_11: NPTH, NPTH, F.Cu at (91.6, 117.3)
- added KiKit_MB_46_12: NPTH, NPTH, F.Cu at (91.9, 117.3)
- added KiKit_MB_46_13: NPTH, NPTH, F.Cu at (92.3, 117.3)
- added KiKit_MB_46_14: NPTH, NPTH, F.Cu at (92.6, 117.3)
- added KiKit_MB_46_15: NPTH, NPTH, F.Cu at (93.0, 117.3)
- added KiKit_MB_46_2: NPTH, NPTH, F.Cu at (88.4, 117.3)
- added KiKit_MB_46_3: NPTH, NPTH, F.Cu at (88.7, 117.3)
- added KiKit_MB_46_4: NPTH, NPTH, F.Cu at (89.1, 117.3)
- added KiKit_MB_46_5: NPTH, NPTH, F.Cu at (89.4, 117.3)
- added KiKit_MB_46_6: NPTH, NPTH, F.Cu at (89.8, 117.3)
- added KiKit_MB_46_7: NPTH, NPTH, F.Cu at (90.1, 117.3)
- added KiKit_MB_46_8: NPTH, NPTH, F.Cu at (90.5, 117.3)
- added KiKit_MB_46_9: NPTH, NPTH, F.Cu at (90.9, 117.3)
- added KiKit_MB_47_1: NPTH, NPTH, F.Cu at (204.0, 28.0)
- added KiKit_MB_47_10: NPTH, NPTH, F.Cu at (207.2, 28.0)
- added KiKit_MB_47_11: NPTH, NPTH, F.Cu at (207.6, 28.0)
- added KiKit_MB_47_12: NPTH, NPTH, F.Cu at (207.9, 28.0)
- added KiKit_MB_47_13: NPTH, NPTH, F.Cu at (208.3, 28.0)
- added KiKit_MB_47_14: NPTH, NPTH, F.Cu at (208.6, 28.0)
- added KiKit_MB_47_15: NPTH, NPTH, F.Cu at (209.0, 28.0)
- added KiKit_MB_47_2: NPTH, NPTH, F.Cu at (204.4, 28.0)
- added KiKit_MB_47_3: NPTH, NPTH, F.Cu at (204.7, 28.0)
- added KiKit_MB_47_4: NPTH, NPTH, F.Cu at (205.1, 28.0)
- added KiKit_MB_47_5: NPTH, NPTH, F.Cu at (205.4, 28.0)
- added KiKit_MB_47_6: NPTH, NPTH, F.Cu at (205.8, 28.0)
- added KiKit_MB_47_7: NPTH, NPTH, F.Cu at (206.1, 28.0)
- added KiKit_MB_47_8: NPTH, NPTH, F.Cu at (206.5, 28.0)
- added KiKit_MB_47_9: NPTH, NPTH, F.Cu at (206.9, 28.0)
- added KiKit_MB_48_1: NPTH, NPTH, F.Cu at (204.0, 117.3)
- added KiKit_MB_48_10: NPTH, NPTH, F.Cu at (207.2, 117.3)
- added KiKit_MB_48_11: NPTH, NPTH, F.Cu at (207.6, 117.3)
- added KiKit_MB_48_12: NPTH, NPTH, F.Cu at (207.9, 117.3)
- added KiKit_MB_48_13: NPTH, NPTH, F.Cu at (208.3, 117.3)
- added KiKit_MB_48_14: NPTH, NPTH, F.Cu at (208.6, 117.3)
- added KiKit_MB_48_15: NPTH, NPTH, F.Cu at (209.0, 117.3)
- added KiKit_MB_48_2: NPTH, NPTH, F.Cu at (204.4, 117.3)
- added KiKit_MB_48_3: NPTH, NPTH, F.Cu at (204.7, 117.3)
- added KiKit_MB_48_4: NPTH, NPTH, F.Cu at (205.1, 117.3)
- added KiKit_MB_48_5: NPTH, NPTH, F.Cu at (205.4, 117.3)
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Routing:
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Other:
- board size 105 x 103.3 mm -> 121 x 105.3 mm
- board text added: "VCC TX RX GND NFC"
- board text added: "v 1.0 Made in Germany 11/24"
- board text removed: "VCC TX RX GND"
- board text removed: "v 0.9 pre-production 09/24"

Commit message: new panel
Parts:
- removed the D1 at (106.1, 104.4)
- removed the D1 at (127.7, 104.4)
- removed the D1 at (149.3, 104.4)
- removed the D1 at (106.1, 58.3)
- removed the D1 at (170.9, 58.3)
- removed the D1 at (192.5, 104.4)
- removed the D1 at (149.3, 58.3)
- removed the D1 at (127.7, 58.3)
- removed the D1 at (192.5, 58.3)
- removed the D1 at (170.9, 104.4)
- removed the D2 at (147.7, 58.3)
- removed the D2 at (169.3, 58.3)
- removed the D2 at (147.7, 104.4)
- removed the D2 at (126.1, 104.4)
- removed the D2 at (190.9, 104.4)
- removed the D2 at (104.5, 104.4)
- removed the D2 at (104.5, 58.3)
- removed the D2 at (126.1, 58.3)
- removed the D2 at (190.9, 58.3)
- removed the D2 at (169.3, 104.4)
- removed the R1 at (194.2, 44.7)
- removed the R1 at (151.0, 44.7)
- removed the R1 at (194.2, 90.8)
- removed the R1 at (151.0, 90.8)
- removed the R1 at (172.6, 44.7)
- removed the R1 at (107.8, 44.7)
- removed the R1 at (129.4, 90.8)
- removed the R1 at (129.4, 44.7)
- removed the R1 at (172.6, 90.8)
- removed the R1 at (107.8, 90.8)
- removed the R2 at (194.2, 47.1)
- removed the R2 at (172.6, 47.1)
- removed the R2 at (151.0, 47.1)
- removed the R2 at (107.8, 47.1)
- removed the R2 at (172.6, 93.2)
- removed the R2 at (151.0, 93.2)
- removed the R2 at (194.2, 93.2)
- removed the R2 at (107.8, 93.2)
- removed the R2 at (129.4, 47.1)
- removed the R2 at (129.4, 93.2)
- removed the U2 at (151.5, 99.0)
- removed the U2 at (129.9, 52.9)
- removed the U2 at (151.5, 52.9)
- removed the U2 at (108.3, 99.0)
- removed the U2 at (173.1, 52.9)
- removed the U2 at (173.1, 99.0)
- removed the U2 at (194.7, 99.0)
- removed the U2 at (108.3, 52.9)
- removed the U2 at (129.9, 99.0)
- removed the U2 at (194.7, 52.9)
- removed the U3 at (124.7, 92.6)
- removed the U3 at (189.6, 46.5)
- removed the U3 at (146.4, 46.5)
- removed the U3 at (168.0, 92.6)
- removed the U3 at (168.0, 46.5)
- removed the U3 at (189.6, 92.6)
- removed the U3 at (103.1, 46.5)
- removed the U3 at (124.7, 46.5)
- removed the U3 at (103.1, 92.6)
- removed the U3 at (146.4, 92.6)
- added D1: CDBU0130L, Diode_SMD:D_0603_1608Metric, F.Cu at (127.7, 104.4)
- added D1: CDBU0130L, Diode_SMD:D_0603_1608Metric, F.Cu at (192.5, 58.3)
- added D1: CDBU0130L, Diode_SMD:D_0603_1608Metric, F.Cu at (106.1, 58.3)
- added D1: CDBU0130L, Diode_SMD:D_0603_1608Metric, F.Cu at (170.9, 104.4)
- added D1: CDBU0130L, Diode_SMD:D_0603_1608Metric, F.Cu at (106.1, 104.4)
- added D1: CDBU0130L, Diode_SMD:D_0603_1608Metric, F.Cu at (192.5, 104.4)
- added D1: CDBU0130L, Diode_SMD:D_0603_1608Metric, F.Cu at (170.9, 58.3)
- added D1: CDBU0130L, Diode_SMD:D_0603_1608Metric, F.Cu at (149.3, 58.3)
- added D1: CDBU0130L, Diode_SMD:D_0603_1608Metric, F.Cu at (127.7, 58.3)
- added D1: CDBU0130L, Diode_SMD:D_0603_1608Metric, F.Cu at (149.3, 104.4)
- added D2: CDBU0130L, Diode_SMD:D_0603_1608Metric, F.Cu at (104.5, 104.4)
- added D2: CDBU0130L, Diode_SMD:D_0603_1608Metric, F.Cu at (147.7, 104.4)
- added D2: CDBU0130L, Diode_SMD:D_0603_1608Metric, F.Cu at (126.1, 58.3)
- added D2: CDBU0130L, Diode_SMD:D_0603_1608Metric, F.Cu at (190.9, 104.4)
- added D2: CDBU0130L, Diode_SMD:D_0603_1608Metric, F.Cu at (169.3, 104.4)
- added D2: CDBU0130L, Diode_SMD:D_0603_1608Metric, F.Cu at (169.3, 58.3)
- added D2: CDBU0130L, Diode_SMD:D_0603_1608Metric, F.Cu at (147.7, 58.3)
- added D2: CDBU0130L, Diode_SMD:D_0603_1608Metric, F.Cu at (104.5, 58.3)
- added D2: CDBU0130L, Diode_SMD:D_0603_1608Metric, F.Cu at (126.1, 104.4)
- added D2: CDBU0130L, Diode_SMD:D_0603_1608Metric, F.Cu at (190.9, 58.3)
- added R1: 4.7k, Resistor_SMD:R_0603_1608Metric, F.Cu at (129.4, 90.8)
- added R1: 4.7k, Resistor_SMD:R_0603_1608Metric, F.Cu at (129.4, 44.7)
- added R1: 4.7k, Resistor_SMD:R_0603_1608Metric, F.Cu at (172.6, 44.7)
- added R1: 4.7k, Resistor_SMD:R_0603_1608Metric, F.Cu at (194.2, 90.8)
- added R1: 4.7k, Resistor_SMD:R_0603_1608Metric, F.Cu at (172.6, 90.8)
- added R1: 4.7k, Resistor_SMD:R_0603_1608Metric, F.Cu at (194.2, 44.7)
- added R1: 4.7k, Resistor_SMD:R_0603_1608Metric, F.Cu at (107.8, 90.8)
- added R1: 4.7k, Resistor_SMD:R_0603_1608Metric, F.Cu at (107.8, 44.7)
- added R1: 4.7k, Resistor_SMD:R_0603_1608Metric, F.Cu at (151.0, 90.8)
- added R1: 4.7k, Resistor_SMD:R_0603_1608Metric, F.Cu at (151.0, 44.7)
- added R2: 4.7k, Resistor_SMD:R_0603_1608Metric, F.Cu at (107.8, 93.2)
- added R2: 4.7k, Resistor_SMD:R_0603_1608Metric, F.Cu at (151.0, 47.1)
- added R2: 4.7k, Resistor_SMD:R_0603_1608Metric, F.Cu at (107.8, 47.1)
- added R2: 4.7k, Resistor_SMD:R_0603_1608Metric, F.Cu at (129.4, 47.1)
- added R2: 4.7k, Resistor_SMD:R_0603_1608Metric, F.Cu at (172.6, 47.1)
- added R2: 4.7k, Resistor_SMD:R_0603_1608Metric, F.Cu at (194.2, 93.2)
- added R2: 4.7k, Resistor_SMD:R_0603_1608Metric, F.Cu at (129.4, 93.2)
- added R2: 4.7k, Resistor_SMD:R_0603_1608Metric, F.Cu at (172.6, 93.2)
- added R2: 4.7k, Resistor_SMD:R_0603_1608Metric, F.Cu at (151.0, 93.2)
- added R2: 4.7k, Resistor_SMD:R_0603_1608Metric, F.Cu at (194.2, 47.1)
- added U2: RF430CL330HIRGTR‎, unsurv_offline_pcb_footprints:RF430_3x3mm_regular, F.Cu at (129.9, 52.9)
- added U2: RF430CL330HIRGTR‎, unsurv_offline_pcb_footprints:RF430_3x3mm_regular, F.Cu at (173.1, 52.9)
- added U2: RF430CL330HIRGTR‎, unsurv_offline_pcb_footprints:RF430_3x3mm_regular, F.Cu at (108.3, 99.0)
- added U2: RF430CL330HIRGTR‎, unsurv_offline_pcb_footprints:RF430_3x3mm_regular, F.Cu at (173.1, 99.0)
- added U2: RF430CL330HIRGTR‎, unsurv_offline_pcb_footprints:RF430_3x3mm_regular, F.Cu at (129.9, 99.0)
- added U2: RF430CL330HIRGTR‎, unsurv_offline_pcb_footprints:RF430_3x3mm_regular, F.Cu at (151.5, 52.9)
- added U2: RF430CL330HIRGTR‎, unsurv_offline_pcb_footprints:RF430_3x3mm_regular, F.Cu at (108.3, 52.9)
- added U2: RF430CL330HIRGTR‎, unsurv_offline_pcb_footprints:RF430_3x3mm_regular, F.Cu at (194.7, 52.9)
- added U2: RF430CL330HIRGTR‎, unsurv_offline_pcb_footprints:RF430_3x3mm_regular, F.Cu at (151.5, 99.0)
- added U2: RF430CL330HIRGTR‎, unsurv_offline_pcb_footprints:RF430_3x3mm_regular, F.Cu at (194.7, 99.0)
- added U3: ATtiny1626-MFR, unsurv_offline_pcb_footprints:VQFN-20-1EP_3x3mm_P0.4mm_EP1.7x1.7mm_edited, F.Cu at (168.0, 92.6)
- added U3: ATtiny1626-MFR, unsurv_offline_pcb_footprints:VQFN-20-1EP_3x3mm_P0.4mm_EP1.7x1.7mm_edited, F.Cu at (124.7, 46.5)
- added U3: ATtiny1626-MFR, unsurv_offline_pcb_footprints:VQFN-20-1EP_3x3mm_P0.4mm_EP1.7x1.7mm_edited, F.Cu at (103.1, 46.5)
- added U3: ATtiny1626-MFR, unsurv_offline_pcb_footprints:VQFN-20-1EP_3x3mm_P0.4mm_EP1.7x1.7mm_edited, F.Cu at (189.6, 46.5)
- added U3: ATtiny1626-MFR, unsurv_offline_pcb_footprints:VQFN-20-1EP_3x3mm_P0.4mm_EP1.7x1.7mm_edited, F.Cu at (146.4, 92.6)
- added U3: ATtiny1626-MFR, unsurv_offline_pcb_footprints:VQFN-20-1EP_3x3mm_P0.4mm_EP1.7x1.7mm_edited, F.Cu at (103.1, 92.6)
- added U3: ATtiny1626-MFR, unsurv_offline_pcb_footprints:VQFN-20-1EP_3x3mm_P0.4mm_EP1.7x1.7mm_edited, F.Cu at (124.7, 92.6)
- added U3: ATtiny1626-MFR, unsurv_offline_pcb_footprints:VQFN-20-1EP_3x3mm_P0.4mm_EP1.7x1.7mm_edited, F.Cu at (146.4, 46.5)
- added U3: ATtiny1626-MFR, unsurv_offline_pcb_footprints:VQFN-20-1EP_3x3mm_P0.4mm_EP1.7x1.7mm_edited, F.Cu at (189.6, 92.6)
- added U3: ATtiny1626-MFR, unsurv_offline_pcb_footprints:VQFN-20-1EP_3x3mm_P0.4mm_EP1.7x1.7mm_edited, F.Cu at (168.0, 46.5)
- C6 (x10): value 47uF -> 100uF
- C7 (x10): value 47uF -> 1uf
